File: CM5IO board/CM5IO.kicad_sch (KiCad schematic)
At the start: 12 parts, among them J11 USB_C_Receptacle_USB2.0

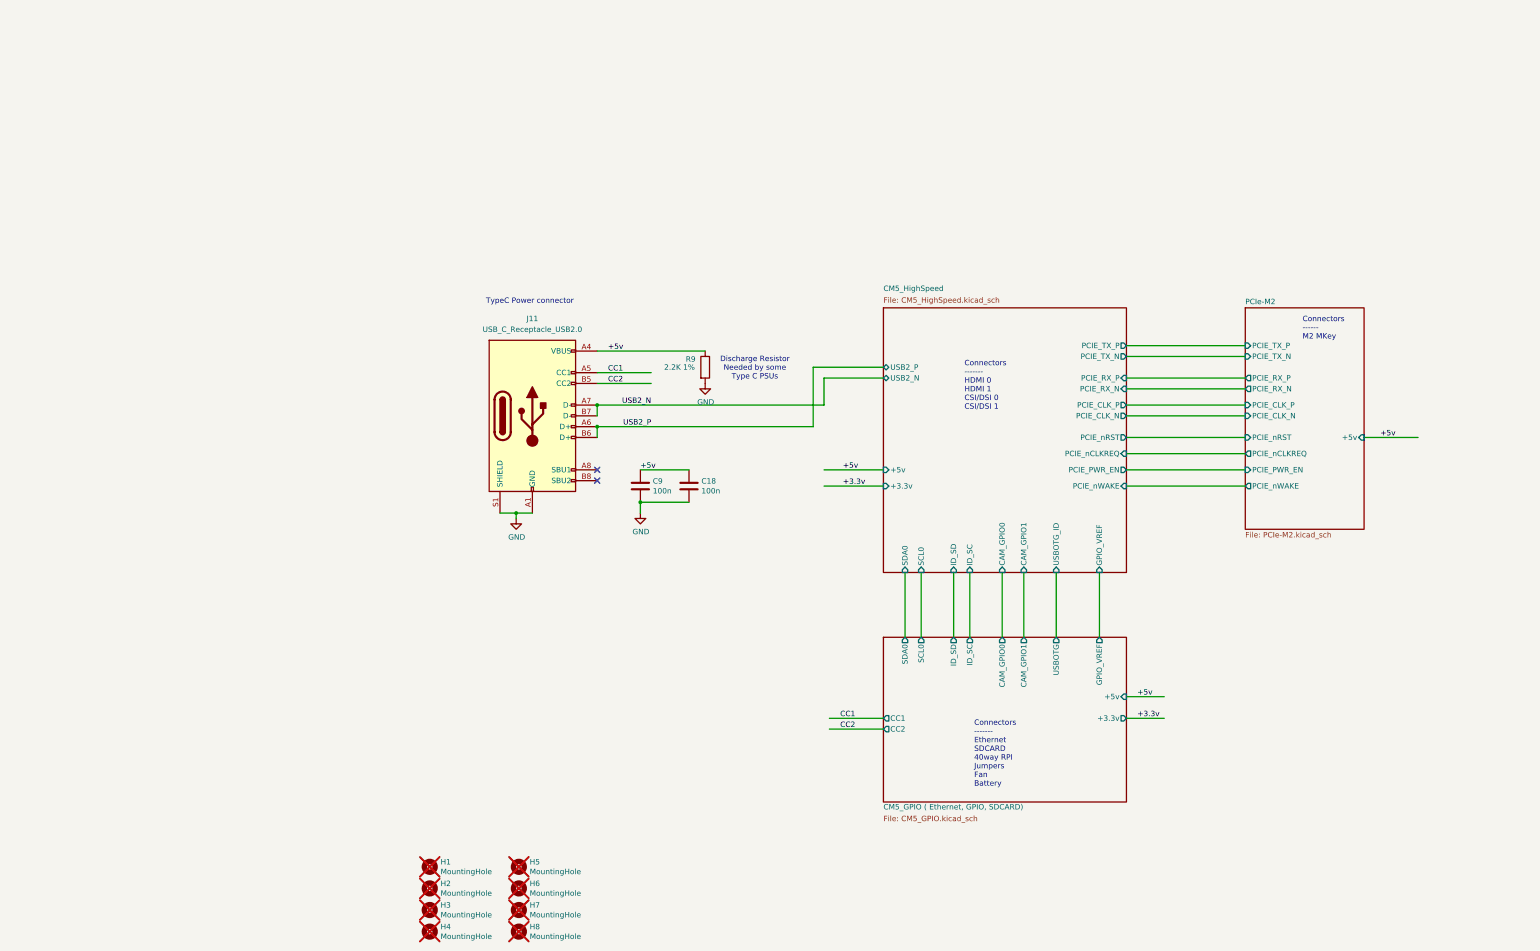
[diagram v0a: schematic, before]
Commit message: Copied Ricardo template on CM5IO board
There's not enough space!!
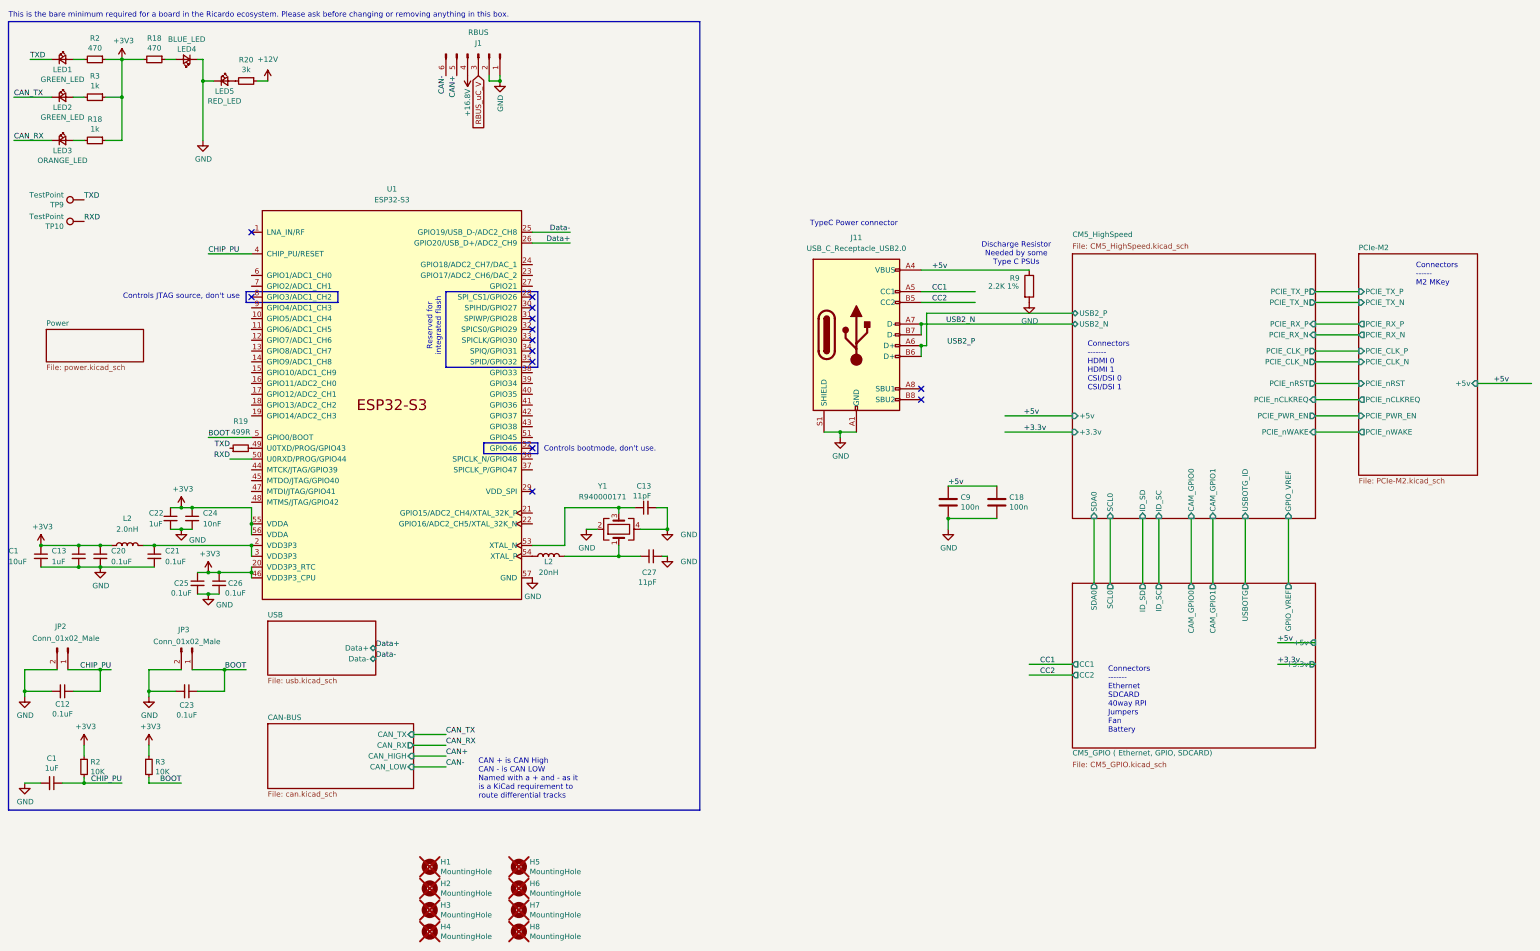
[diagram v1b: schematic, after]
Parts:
- added C1, C13, C22: 1uF, Capacitor_SMD:C_0402_1005Metric, symbol Device:C_Small
- added C1: 10uF, Capacitor_SMD:C_0402_1005Metric, symbol Device:C_Small
- added C12, C20, C21, C23, C25, C26: 0.1uF, Capacitor_SMD:C_0402_1005Metric, symbol Device:C_Small
- added C13, C27: 11pF, Capacitor_SMD:C_0402_1005Metric, symbol Device:C_Small
- added C24: 10nF, Capacitor_SMD:C_0402_1005Metric, symbol Device:C_Small
- added J1: RBUS, iclr:Molex_Mini-Fit_Jr_5569-06A2_2x03_P4.20mm_Horizontal, symbol Connector:Conn_01x06_Male
- added JP2, JP3: Conn_01x02_Male, Connector_PinHeader_2.54mm:PinHeader_1x02_P2.54mm_Vertical, symbol Connector:Conn_01x02_Male
- added L2: 2.0nH, Inductor_SMD:L_0402_1005Metric, symbol Device:L
- added L2: 20nH, Inductor_SMD:L_0402_1005Metric, symbol Device:L
- added LED1, LED2: GREEN_LED, LED_SMD:LED_0402_1005Metric, symbol Device:LED_Small
- added LED3: ORANGE_LED, LED_SMD:LED_0402_1005Metric, symbol Device:LED_Small
- added LED4: BLUE_LED, LED_SMD:LED_0402_1005Metric, symbol Device:LED_Small
- added LED5: RED_LED, LED_SMD:LED_0402_1005Metric, symbol Device:LED_Small
- added R18, R3: 1k, Resistor_SMD:R_0402_1005Metric, symbol Device:R_Small
- added R18, R2: 470, Resistor_SMD:R_0402_1005Metric, symbol Device:R_Small
- added R19: 499R, Resistor_SMD:R_0402_1005Metric, symbol Device:R_Small
- added R2, R3: 10K, Resistor_SMD:R_0402_1005Metric, symbol Device:R_Small
- added R20: 3k, Resistor_SMD:R_0402_1005Metric, symbol Device:R_Small
- added TP10, TP9: TestPoint, TestPoint:TestPoint_Pad_D1.0mm, symbol Connector:TestPoint
- added U1: ESP32-S3, iclr:QFN40P700X700X90-57N, symbol Espressif:ESP32-S3
- added Y1: R940000171, iclr:Crystal_SMD_2016-4Pin_2.0x1.6mm, symbol Device:Crystal_GND24
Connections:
- net GND: now also C1.2, C1.2, C12.2, C13.2, C13.2, C20.2, C21.2, C22.2, C23.2, C24.2, C25.2, C26.2, C27.2, J1.1 (Pin_1), J1.2 (Pin_2), JP2.2 (Pin_2), JP3.2 (Pin_2), LED4.1 (K), LED5.1 (K), U1.57 (GND), Y1.2, Y1.4
- net USB2_P: no longer J11.A6 (D+), J11.B6 (D+)
- new net: LED1.2 (A), R2.2
- new net: LED4.2 (A), R18.1
- new net: LED5.2 (A), R20.2
- new net: LED2.2 (A), R3.2
- new net: C21.1, L2.2, U1.2 (VDD3P3), U1.3 (VDD3P3)
- new net: LED3.2 (A), R18.2
- new net: C27.1, L2.2, Y1.1
- new net: C13.1, U1.53 (XTAL_N), Y1.3
- new net: L2.1, U1.54 (XTAL_P)
- new net: R19.2, U1.49 (U0TXD/PROG/GPIO43)
- new net +12V: R20.1
- new net +16.8V: J1.4 (Pin_4)
- new net +3V3: C1.1, C13.1, C20.1, C22.1, C24.1, C25.1, C26.1, L2.1, R18.1, R18.2, R2.1, R2.1, R3.1, R3.1, U1.20 (VDD3P3_RTC), U1.46 (VDD3P3_CPU), U1.55 (VDDA), U1.56 (VDDA)
- new net BOOT: C23.1, JP3.1 (Pin_1), R3.2, U1.5 (GPIO0/BOOT)
- new net CAN+: J1.5 (Pin_5)
- new net CAN-: J1.6 (Pin_6)
- new net CAN_RX: LED3.1 (K)
- new net CAN_TX: LED2.1 (K)
- new net CHIP_PU: C1.1, C12.1, JP2.1 (Pin_1), R2.2, U1.4 (CHIP_PU/RESET)
- new net CM5_HighSpeed/USB2_P: J11.A6 (D+), J11.B6 (D+)
- new net Data+: U1.26 (GPIO20/USB_D+/ADC2_CH9)
- new net Data-: U1.25 (GPIO19/USB_D-/ADC2_CH8)
- new net RBUS_uC_V: J1.3 (Pin_3)
- new net RXD: TP10.1, U1.50 (U0RXD/PROG/GPIO44)
- new net TXD: LED1.1 (K), R19.1, TP9.1
- no-connect marks 2 -> 13
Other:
- added sheet CAN-BUS (can.kicad_sch)
- added sheet Power (power.kicad_sch)
- added sheet USB (usb.kicad_sch)
- note added: "CAN + is CAN High CAN - is CAN LOW Named with a + and - as it is a KiCad requirement to route differential tracks"
- note added: "Controls JTAG source, don't use"
- note added: "Controls bootmode, don't use."
- note added: "Reserved for integrated flash"
- note added: "This is the bare minimum required for a board in the Ricardo ecosystem. Please ask before changing or removing anything in this box."
- moved on the sheet: C18, C9, J11, R9
